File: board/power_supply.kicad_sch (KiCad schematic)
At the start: 52 parts, among them J1 USB, J2 LiPo, U1 IP5306, U2 TPS562201, U3 RT9069, U4 TPS55340

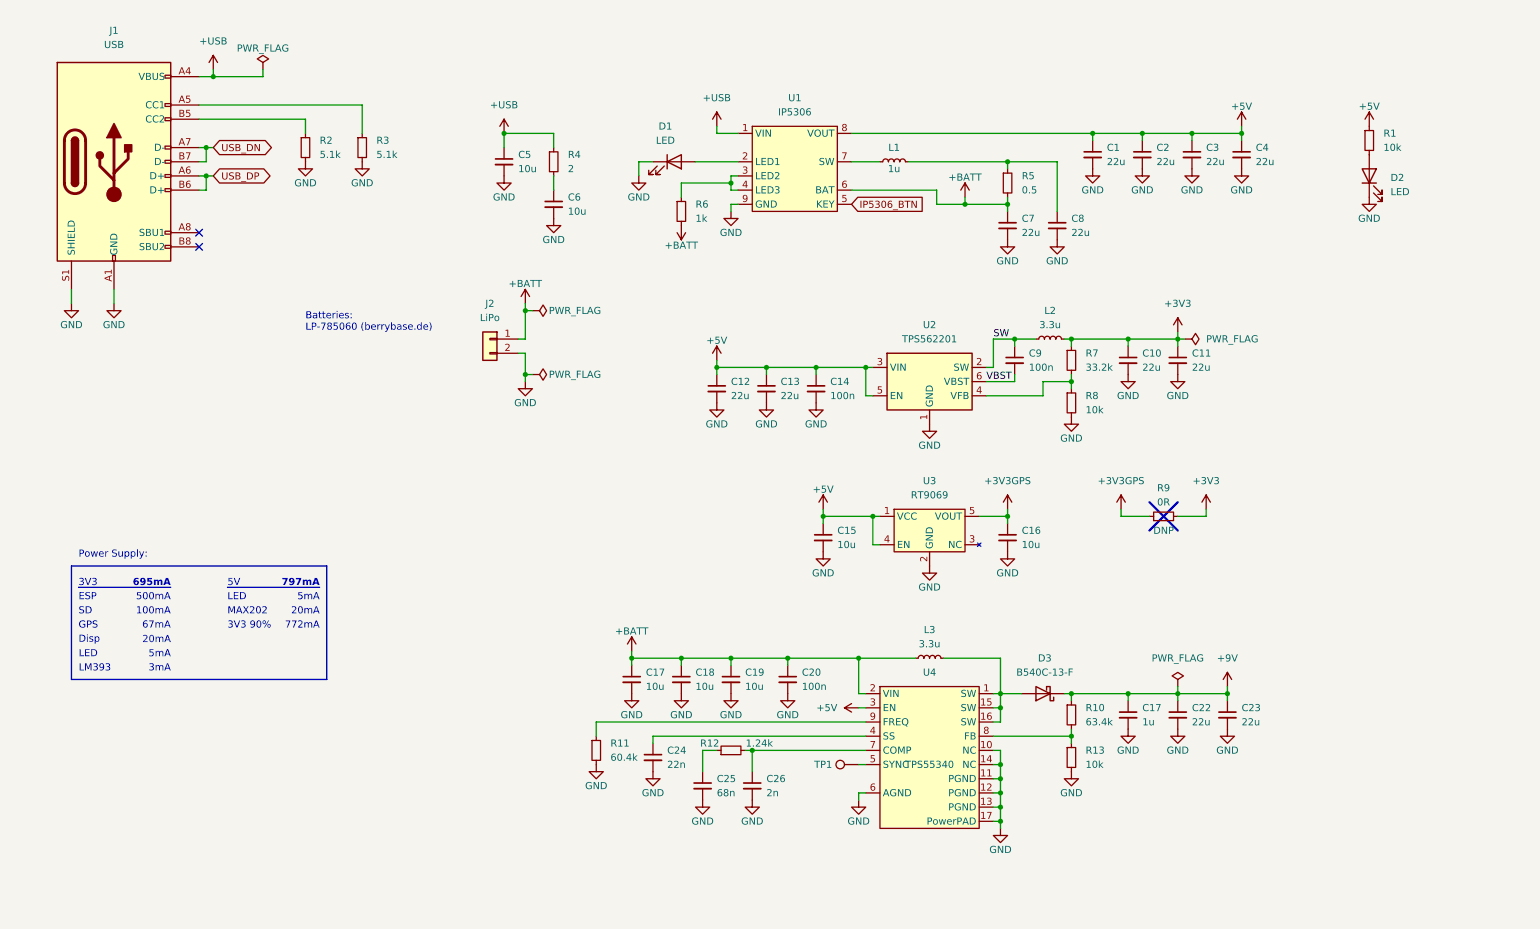
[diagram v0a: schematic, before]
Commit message: Fixed full errata, now v2.1 Most important changes: * Changed power supply architecture * Added hardware ID resistors * Moved USB connector closer to/over the border * Added a 2A fuse * Replaced Beads to display with resistors for better signal integrity * Replaced IP5306 with IP5303 for lower charging current * Switched PGA sensors from TCI to SPI, removed TCI/IO connection * Switched PGA mode from temperature to time decoupling * Added a power-on-reset circuit to keep power-consumption low due to voltage on 5V rail if turned off * Retracted copper planes from the PCB border * Added fabrication output using KiCAD JLCPCB tools
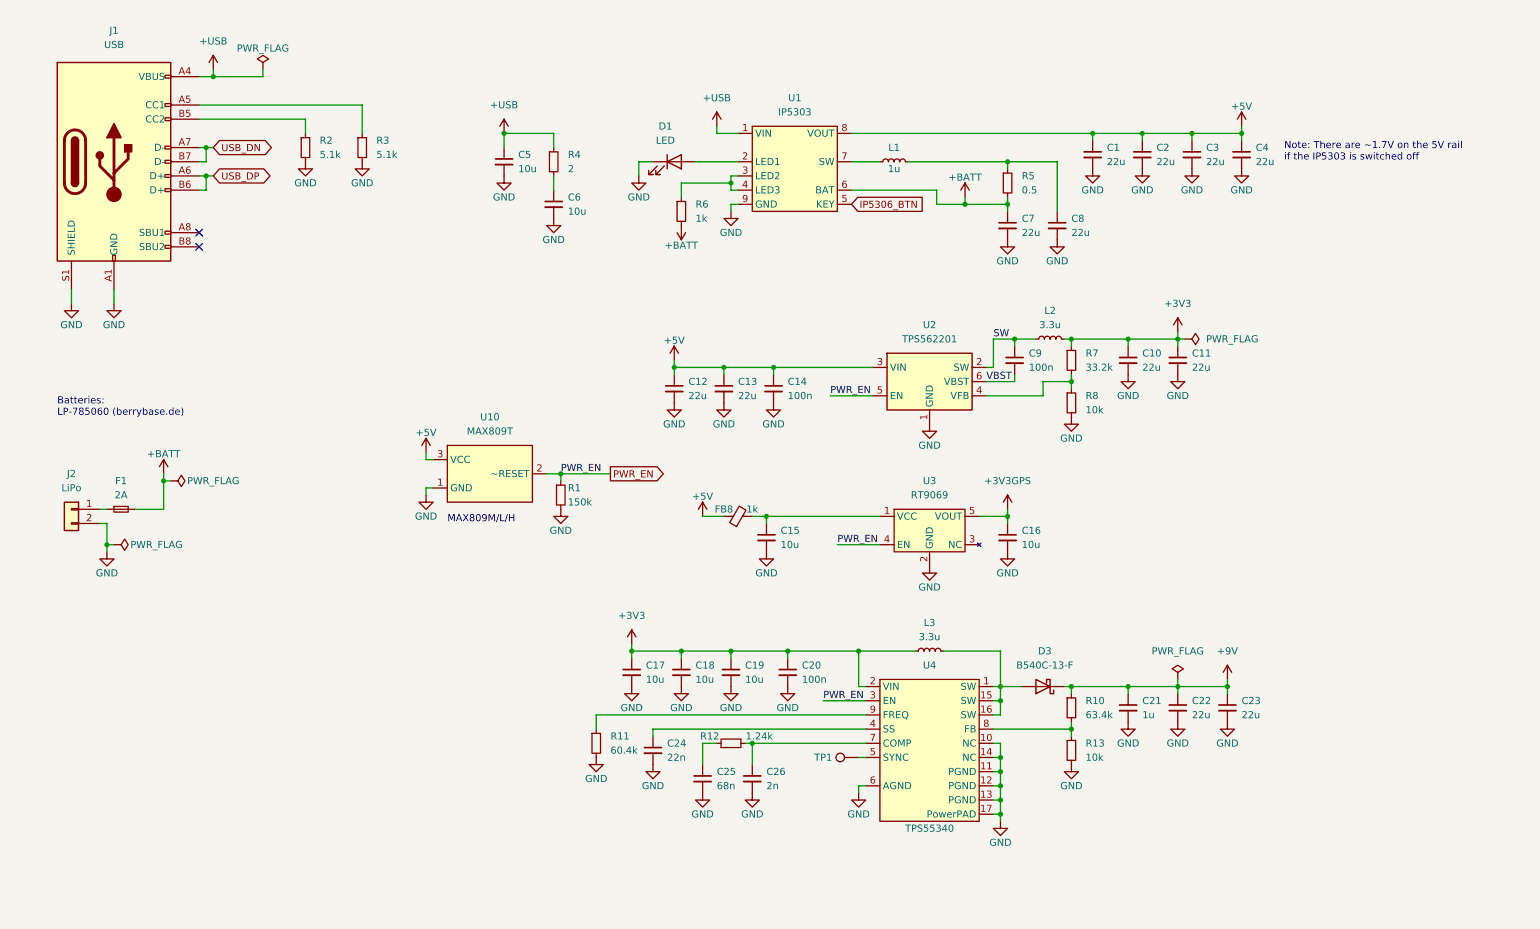
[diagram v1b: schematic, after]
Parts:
- removed D2: LED, LED_SMD:LED_0603_1608Metric, symbol Device:LED
- removed R9: 0R, Resistor_SMD:R_0603_1608Metric, symbol Device:R_Small
- added F1: 2A, Fuse:Fuse_0603_1608Metric, symbol Device:Fuse_Small
- added FB8: 1k, Inductor_SMD:L_0603_1608Metric, symbol Device:FerriteBead_Small
- added U10: MAX809T, Package_TO_SOT_SMD:SOT-23-3, symbol OBSPro:MAX809
- D1: JLC_PN C72043 -> C2286; MPN 19-217/GHC-YR1S2/3T -> KT-0603R; Manufacturer Everlight Elec -> Hubei KENTO Elec
- R1: value 10k -> 150k; JLC_BasicPart yes -> (none); JLC_PN C25804 -> C22807; JLC_Price10 0.0013 -> (none); MPN 0603WAF1002T5E -> 0603WAF1503T5E; PCBA (none) -> yes
- U1: value IP5306 -> IP5303; symbol OBSPro:IP5306 -> OBSPro:IP5303; JLC_PN C181692 -> C181693; JLC_Price10 0.1766 -> 0.3005; MPN IP5306 -> IP5303; kicost:JLC:pricing 1: USD 0.2895; 10: USD 0.2292; 30: USD 0.1998; 100: USD 0.1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 -> (none)
- U4: JLC_BasicPart (none) -> no
- renumbered C17 to C21
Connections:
- net +3V3: now also C17.1, C18.1, C19.1, C20.1, L3.1, U4.2 (VIN)
- net +5V: now also FB8.1, U10.3 (VCC); no longer C15.1, R1.1, U2.5 (EN), U3.1 (VCC), U3.4 (EN), U4.3 (EN)
- net +BATT: now also F1.2; no longer C17.1, C18.1, C19.1, C20.1, J2.1 (Pin_1), L3.1, U4.2 (VIN)
- net GND: now also R1.2, U10.1 (GND)
- new net: C15.1, FB8.2, U3.1 (VCC)
- new net: F1.1, J2.1 (Pin_1)
- new net PWR_EN: R1.1, U10.2 (~RESET), U2.5 (EN), U3.4 (EN), U4.3 (EN)
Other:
- note added: "MAX809M/L/H"
- note added: "Note: There are ~1.7V on the 5V rail if the IP5303 is switched off"
- note removed: "100mA"
- note removed: "20mA"
- note removed: "3V3"
- note removed: "3V3 90%"
- note removed: "3mA"
- note removed: "500mA"
- note removed: "5V"
- note removed: "5mA"
- note removed: "67mA"
- note removed: "695mA"
- note removed: "772mA"
- note removed: "797mA"
- note removed: "Disp"
- note removed: "ESP"
- note removed: "GPS"
- note removed: "LED"
- note removed: "LM393"
- note removed: "MAX202"
- note removed: "Power Supply:"
- note removed: "SD"
- moved on the sheet: C12, C13, C14, C15, C17, C18, C19, C20, C21, C22, C23, C24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

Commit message: Hardware Revision
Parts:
- removed C10, C11, C12, C13, C22, C23: 22u, Capacitor_SMD:C_1206_3216Metric, symbol Device:C_Small
- removed C14, C20: 100n, Capacitor_SMD:C_0603_1608Metric, symbol Device:C_Small
- removed C17, C18, C19: 10u, Capacitor_SMD:C_0603_1608Metric, symbol Device:C_Small
- removed C21: 1u, Capacitor_SMD:C_0603_1608Metric, symbol Device:C_Small
- removed C24: 22n, Capacitor_SMD:C_0603_1608Metric, symbol Device:C_Small
- removed C25: 68n, Capacitor_SMD:C_0603_1608Metric, symbol Device:C_Small
- removed C26: 2n, Capacitor_SMD:C_0603_1608Metric, symbol Device:C_Small
- removed D3: B540C-13-F, Diode_SMD:D_SMC, symbol Device:D_Schottky
- removed L1: 1u, Inductor_SMD:L_Vishay_IFSC-1515AH_4x4x1.8mm, symbol Device:L_Small
- removed L3: 3.3u, Inductor_SMD:L_Sunlord_MWSA0503S, symbol Device:L_Small
- removed TP1: TestPoint, TestPoint:TestPoint_Pad_1.0x1.0mm, symbol Connector:TestPoint
- removed U1: IP5303, Package_SO:HSOP-8-1EP_3.9x4.9mm_P1.27mm_EP2.3x2.3mm, symbol OBSPro:IP5303
- removed U10: MAX809T, Package_TO_SOT_SMD:SOT-23-3, symbol OBSPro:MAX809
- removed U2: TPS562201, Package_TO_SOT_SMD:SOT-23-6, symbol Regulator_Switching:TPS562200
- removed U4: TPS55340, Package_DFN_QFN:VQFN-16-1EP_3x3mm_P0.5mm_EP1.68x1.68mm, symbol OBSPro:TPS55340R
- added C51: 100n, Capacitor_SMD:C_0603_1608Metric, symbol Device:C_Small
- added D2: LED, LED_SMD:LED_0603_1608Metric, symbol Device:LED
- added D3: D_Small, Diode_SMD:D_SOD-123F, symbol Device:D_Small
- added D6: B540C-13-F, Diode_SMD:D_SMC, symbol Device:D_Schottky
- added J3: On/Off, OpenBikeSensor:Connector_1x02_Switch, symbol Connector:Conn_01x02_Male
- added J5: Temp, Connector_JST:JST_PH_S2B-PH-K_1x02_P2.00mm_Horizontal, symbol Connector_Generic:Conn_01x02
- added L4: 3.3u, symbol Device:L_Small
- added Q10, Q8: SI2302, Package_TO_SOT_SMD:SOT-23, symbol Device:Q_NMOS_GSD
- added R45: 100, Resistor_SMD:R_0603_1608Metric, symbol Device:R_Small
- added R47: 1.24k, Resistor_SMD:R_0603_1608Metric, symbol Device:R_Small
- added R48, R51, R52: 1k, Resistor_SMD:R_0603_1608Metric, symbol Device:R_Small
- added R49: 62k, Resistor_SMD:R_0603_1608Metric, symbol Device:R_Small
- added R50: 100k, Resistor_SMD:R_0603_1608Metric, symbol Device:R_Small
- added R54: 10k, Resistor_SMD:R_0603_1608Metric, symbol Device:R_Small
- added U1: LGS4056HEP, Package_SO:SOP-8-1EP_4.57x4.57mm_P1.27mm_EP4.57x4.45mm, symbol OBSPro:LGS4056HEP
- added U11: FM2113, Package_TO_SOT_SMD:SOT-23-6, symbol OBSPro:FM2113
- added U2: TLV61048, Package_TO_SOT_SMD:SOT-23-6, symbol OBSPro:TLV61048
- added U4: JW5026, Package_TO_SOT_SMD:SOT-23-6, symbol OBSPro:JW5026
- C1, C2, C3, C4: value 22u -> 10u; footprint Capacitor_SMD:C_1206_3216Metric -> Capacitor_SMD:C_0603_1608Metric; JLC_BasicPart no -> yes; JLC_PN C5672 -> C19702; JLC_Price1 (none) -> 0.062; JLC_Price10 0.0217 -> 0.0052; JLC_Price100 (none) -> 0.0031; JLC_Price1000 (none) -> 0.0029; MPN CL31A226KPHNNNE -> CL10A106KP8NNNC; kicost:JLC:pricing 1: USD 0.0192; 150: USD 0.0186 -> 1: USD 0.062; 10: USD 0.0062; 100: USD 0.0031; 1000: USD 0.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
- C7: value 22u -> 1u; footprint Capacitor_SMD:C_1206_3216Metric -> Capacitor_SMD:C_0603_1608Metric; JLC_BasicPart no -> yes; JLC_PN C5672 -> C15849; JLC_Price1 (none) -> 0.056; JLC_Price10 0.0217 -> 0.0051; JLC_Price100 (none) -> 0.0028; JLC_Price1000 (none) -> 0.0027; MPN CL31A226KPHNNNE -> CL10A105KB8NNNC; kicost:JLC:pricing 1: USD 0.0192; 150: USD 0.0186 -> 1: USD 0.056; 10: USD 0.0056; 100: USD 0.0028; 1000: USD 0.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
- C8: value 22u -> 100n; footprint Capacitor_SMD:C_1206_3216Metric -> Capacitor_SMD:C_0603_1608Metric; JLC_BasicPart no -> yes; JLC_PN C5672 -> C14663; JLC_Price1 (none) -> 0.042; JLC_Price10 0.0217 -> 0.0021; JLC_Price100 (none) -> 0.0021; JLC_Price1000 (none) -> 0.0014; MPN CL31A226KPHNNNE -> CC0603KRX7R9BB104; Manufacturer Samsung Electro-Mechanics -> YAGEO; kicost:JLC:pricing 1: USD 0.0192; 150: USD 0.0186 -> 1: USD 0.0020; 200: USD 0.0016; 800: USD 0.0013; 1600: USD 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
- C9: value 100n -> 10u; JLC_PN C14663 -> C19702; JLC_Price1 0.042 -> 0.062; JLC_Price10 0.0021 -> 0.0052; JLC_Price100 0.0021 -> 0.0031; JLC_Price1000 0.0014 -> 0.0029; MPN CC0603KRX7R9BB104 -> CL10A106KP8NNNC; Manufacturer YAGEO -> Samsung Electro-Mechanics; kicost:JLC:pricing 1: USD 0.0020; 200: USD 0.0016; 800: USD 0.0013; 1600: USD 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 -> 1: USD 0.062; 10: USD 0.0062; 100: USD 0.0031; 1000: USD 0.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
- F1: value 2A -> 1A; JLC_PN C187605 -> C151139; MPN 0467002.NRHF -> 0467001.NRHF
- L2: value 3.3u -> 10u; footprint Inductor_SMD:L_Vishay_IFSC-1515AH_4x4x1.8mm -> (none); JLC_BasicPart no -> (none); JLC_PN C98362 -> (none); JLC_Price10 0.0766 -> (none); MPN WPN4020H3R3MT -> FNR6045S100MT; Manufacturer Sunlord -> cjiang
- R1: value 150k -> 100k; JLC_BasicPart (none) -> yes; JLC_PN C22807 -> (none); MPN 0603WAF1503T5E -> 0603WAF1003T5E
- R10: value 63.4k -> 5.1k; JLC_BasicPart no -> yes; JLC_PN C23093 -> C23186; JLC_Price10 (none) -> 0.0009; MPN 0603WAF6342T5E -> 0603WAF5101T5E; PCBA (none) -> yes; kicost:JLC:pricing (none) -> 1: USD 0.0009; 200: USD 0.0007; 1000: USD 0.0006; 10000: US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
- R11: value 60.4k -> 2.7k; JLC_BasicPart no -> yes; JLC_PN C23089 -> C13167; MPN 0603WAF6042T5E -> 0603WAF2701T5E
- R13: value 10k -> 1.24k; JLC_BasicPart yes -> no; JLC_PN C25804 -> C25956; JLC_Price10 0.0013 -> (none); MPN 0603WAF1002T5E -> 0603WAF1241T5E; Manufacturer UNI-ROYAL(Uniroyal Elec) -> UNI-ROYAL(Uniroyal Elec)
- R5: value 0.5 -> 2; JLC_BasicPart no -> yes; JLC_PN C45312 -> C22977; JLC_Price10 0.0025 -> 0.0012; MPN 0603WAF500LT5E -> 0603WAF200KT5E; kicost:JLC:pricing 1: USD 0.0044; 200: USD 0.0037; 1000: USD 0.0033; 2000: USD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 -> 1: USD 0.0014; 200: USD 0.0011; 1000: USD 0.0009
- R6: value 1k -> 2; JLC_PN C21190 -> C22977; JLC_Price10 0.0005 -> 0.0012; MPN 0603WAF1001T5E -> 0603WAF200KT5E; kicost:JLC:pricing 1: USD 0.0005; 200: USD 0.0004 -> 1: USD 0.0014; 200: USD 0.0011; 1000: USD 0.0009
- R7: value 33.2k -> 100k; JLC_BasicPart no -> yes; JLC_PN C23003 -> (none); JLC_Price10 0.0009 -> (none); MPN 0603WAF3322T5E -> 0603WAF1003T5E; PCBA (none) -> yes
- R8: value 10k -> 2.7k; JLC_PN C25804 -> C13167; JLC_Price10 0.0013 -> (none); MPN 0603WAF1002T5E -> 0603WAF2701T5E
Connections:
- net VBST is gone; now on net +3V3: C9.2
- net +3V3: now also R11.2; no longer R7.1
- net +9V: now also C1.2, C4.2, FB8.1, R1.2, R7.2, U3.4 (EN), D6.1 (K), U4.5 (VIN); no longer R10.1
- net +BATT: now also C3.1, J3.1 (Pin_1), L4.2, R45.2, U1.5 (BAT), U2.4 (EN), U2.5 (VIN); no longer F1.2, R5.2, R6.2
- net +USB: now also R5.1, R6.1, R50.1, R51.1, R52.1, U1.4 (VCC), U1.8 (CE)
- net GND: now also C1.1, C2.1, C4.1, C9.1, R12.1, J5.2 (Pin_2), Q10.2 (S), R47.1, R48.2, R54.2, U1.3 (GND), U1.EP, U2.2 (GND), U2.6 (FREQ), U4.2 (GND); no longer C1.2, C2.2, C4.2, C8.2, D1.1 (K), J2.2 (Pin_2), R1.2, R11.2, R13.2, R8.2
- net at R12.2: now also R13.1
- net at C8.1: now also U4.1 (BST); no longer R5.1
- net at R10.2: now also R11.1; no longer R13.1
- net at D1.2 (A): now also R51.2
- net at R8.1: now also R54.1, U2.3 (FB); no longer R7.2
- removed net +5V: C1.1, C2.1, C3.1, C4.1, FB8.1
- net PWR_EN: no longer names the net of R1.1
- net PWR_EN: now also R8.2; no longer U3.4 (EN)
- net SW: no longer names the net of L2.1
- net SW: now also C8.2, U4.6 (SW); no longer C9.1
- new net: Q8.1 (G), U11.1 (OD)
- new net: Q10.3 (D), Q8.3 (D)
- new net: R49.1, R50.2, U1.1 (TEMP)
- new net: Q10.1 (G), U11.3 (OC)
- new net: R48.1, U1.2 (PROG)
- new net: D2.1 (K), U1.6 (DONE)
- new net: D1.1 (K), U1.7 (CHRG)
- new net: C51.1, R45.1, U11.5 (VDD)
- new net: C51.2, U11.6 (VSS)
- new net: J5.1 (Pin_1), R49.2
- new net: D3.1 (K), F1.2, J3.2 (Pin_2)
- new net: C2.2, R5.2, R6.2
- new net: R47.2, U11.2 (CS)
- new net: D6.2 (A), L4.1, U2.1 (SW)
- new net: D2.2 (A), R52.2
- new net: R7.1, U4.4 (EN)
- new net: R10.1, R13.2, U4.3 (FB)
- new net -BATT: D3.2 (A), J2.2 (Pin_2), Q8.2 (S)
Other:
- note added: "BATT CONNECTOR"
- note added: "BATT PROTECTION CIRCUIT"
- note added: "BOOST 9V"
- note added: "BUCK 3V3 GENERAL"
- note added: "CHARGE CIRCUIT"
- note added: "LDO 3V3 GPS"
- note added: "USB CONNECTOR"
- note removed: "MAX809M/L/H"
- note removed: "Note: There are ~1.7V on the 5V rail if the IP5303 is switched off"
- moved on the sheet: C15, C16, C5, C6, D1, F1, FB8, J1, J2, R2, R3, U3
